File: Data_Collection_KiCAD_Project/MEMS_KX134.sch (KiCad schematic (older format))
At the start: 2 parts

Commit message: Fixed Component Libraries
Changed over from project specific to global libraries.
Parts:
- C?: symbol Data_Collection_KiCAD_Project-rescue:C_Small-Device -> Data_Collection_KiCAD_Project-rescue:C_Small-Device-Data_Collection_KiCAD_Project-rescue
- U?: symbol Data_Collection_KiCAD_Project-rescue:KX122-1042-Sensor_Motion -> Data_Collection_KiCAD_Project-rescue:KX122-1042-Sensor_Motion-Data_Collection_KiCAD_Project-rescue
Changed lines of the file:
@@
 $Descr A4 11693 8268
 encoding utf-8
-Sheet 9 10
+Sheet 9 9
 Title "ICM-20948 MEMS Chip"
 Date "2021-10-01"
@@
 $EndDescr
 $Comp
-L Data_Collection_KiCAD_Project-rescue:KX122-1042-Sensor_Motion U?
+L Data_Collection_KiCAD_Project-rescue:KX122-1042-Sensor_Motion-Data_Collection_KiCAD_Project-rescue U?
 U 1 1 6165C3D0
 P 5950 3450
@@
 SCL
 $Comp
-L Data_Collection_KiCAD_Project-rescue:GND-power #PWR?
+L Data_Collection_KiCAD_Project-rescue:GND-power-Data_Collection_KiCAD_Project-rescue #PWR?
 U 1 1 61692503
 P 5950 3950
@@
 $EndComp
 $Comp
-L Data_Collection_KiCAD_Project-rescue:+3.3V-power #PWR?
+L Data_Collection_KiCAD_Project-rescue:+3.3V-power-Data_Collection_KiCAD_Project-rescue #PWR?
 U 1 1 6169CC30
 P 5350 2900
@@
 $EndComp
 $Comp
-L Data_Collection_KiCAD_Project-rescue:C_Small-Device C?
+L Data_Collection_KiCAD_Project-rescue:C_Small-Device-Data_Collection_KiCAD_Project-rescue C?
 U 1 1 6169DA95
 P 6450 2900
@@
 $EndComp
 $Comp
-L Data_Collection_KiCAD_Project-rescue:GND-power #PWR?
+L Data_Collection_KiCAD_Project-rescue:GND-power-Data_Collection_KiCAD_Project-rescue #PWR?
 U 1 1 6169E39E
 P 6650 2900
@@
 KX134-1211 I2C Addresses:\nADDR = 0 -> 0x1E\nADDR = 1 -> 0x1F
 $Comp
-L Data_Collection_KiCAD_Project-rescue:GND-power #PWR?
+L Data_Collection_KiCAD_Project-rescue:GND-power-Data_Collection_KiCAD_Project-rescue #PWR?
 U 1 1 616ACA8D
 P 5200 3600
@@
 	5200 3450 5200 3600
 $Comp
-L Data_Collection_KiCAD_Project-rescue:GND-power #PWR?
+L Data_Collection_KiCAD_Project-rescue:GND-power-Data_Collection_KiCAD_Project-rescue #PWR?
 U 1 1 616AF0ED
 P 6700 3900

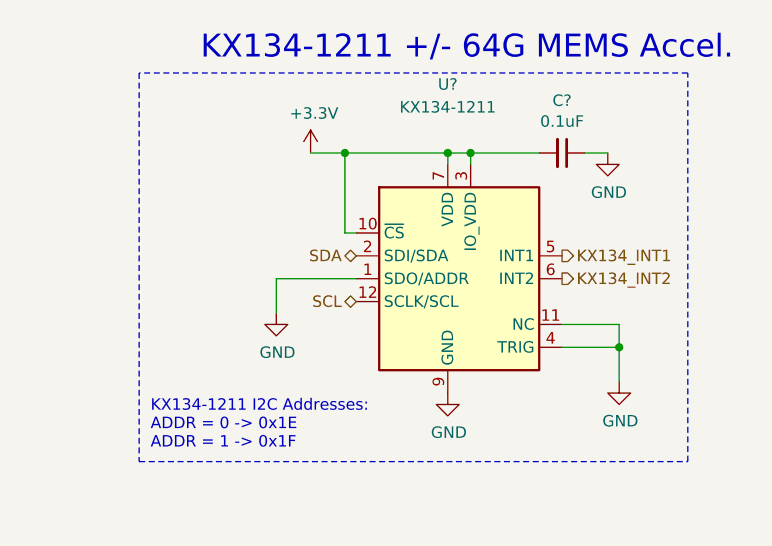
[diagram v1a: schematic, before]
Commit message: footprint and value changes
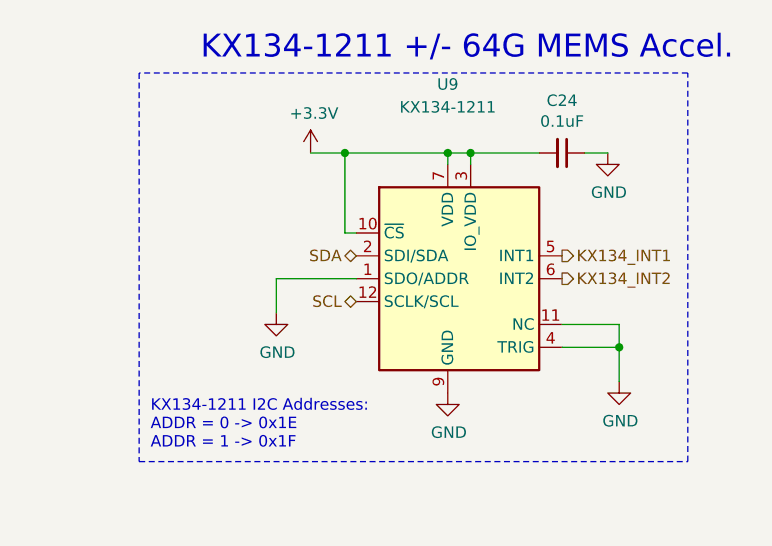
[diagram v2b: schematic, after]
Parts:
- C24: renamed from C?; footprint (none) -> Capacitor_SMD:C_0603_1608Metric
- gave numbers to parts that had none: 1
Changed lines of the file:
@@
 $EndDescr
 $Comp
-L Data_Collection_KiCAD_Project-rescue:KX122-1042-Sensor_Motion-Data_Collection_KiCAD_Project-rescue U?
+L Data_Collection_KiCAD_Project-rescue:KX122-1042-Sensor_Motion-Data_Collection_KiCAD_Project-rescue U9
 U 1 1 6165C3D0
 P 5950 3450
-F 0 "U?" H 5950 4300 50  0000 C CNN
+F 0 "U9" H 5950 4300 50  0000 C CNN
 F 1 "KX134-1211" H 5950 4200 50  0000 C CNN
 F 2 "Package_LGA:LGA-12_2x2mm_P0.5mm" H 6100 4000 50  0001 L CNN
@@
 SCL
 $Comp
-L Data_Collection_KiCAD_Project-rescue:GND-power-Data_Collection_KiCAD_Project-rescue #PWR?
+L Data_Collection_KiCAD_Project-rescue:GND-power-Data_Collection_KiCAD_Project-rescue #PWR056
 U 1 1 61692503
 P 5950 3950
-F 0 "#PWR?" H 5950 3700 50  0001 C CNN
+F 0 "#PWR056" H 5950 3700 50  0001 C CNN
 F 1 "GND" H 5955 3777 50  0000 C CNN
 F 2 "" H 5950 3950 50  0001 C CNN
@@
 $EndComp
 $Comp
-L Data_Collection_KiCAD_Project-rescue:+3.3V-power-Data_Collection_KiCAD_Project-rescue #PWR?
+L Data_Collection_KiCAD_Project-rescue:+3.3V-power-Data_Collection_KiCAD_Project-rescue #PWR055
 U 1 1 6169CC30
 P 5350 2900
-F 0 "#PWR?" H 5350 2750 50  0001 C CNN
+F 0 "#PWR055" H 5350 2750 50  0001 C CNN
 F 1 "+3.3V" H 5365 3073 50  0000 C CNN
 F 2 "" H 5350 2900 50  0001 C CNN
@@
 $EndComp
 $Comp
-L Data_Collection_KiCAD_Project-rescue:C_Small-Device-Data_Collection_KiCAD_Project-rescue C?
+L Data_Collection_KiCAD_Project-rescue:C_Small-Device-Data_Collection_KiCAD_Project-rescue C24
 U 1 1 6169DA95
 P 6450 2900
-F 0 "C?" V 6221 2900 50  0000 C CNN
+F 0 "C24" V 6221 2900 50  0000 C CNN
 F 1 "0.1uF" V 6312 2900 50  0000 C CNN
-F 2 "" H 6450 2900 50  0001 C CNN
+F 2 "Capacitor_SMD:C_0603_1608Metric" H 6450 2900 50  0001 C CNN
 F 3 "~" H 6450 2900 50  0001 C CNN
 	1    6450 2900
@@
 $EndComp
 $Comp
-L Data_Collection_KiCAD_Project-rescue:GND-power-Data_Collection_KiCAD_Project-rescue #PWR?
+L Data_Collection_KiCAD_Project-rescue:GND-power-Data_Collection_KiCAD_Project-rescue #PWR057
 U 1 1 6169E39E
 P 6650 2900
-F 0 "#PWR?" H 6650 2650 50  0001 C CNN
+F 0 "#PWR057" H 6650 2650 50  0001 C CNN
 F 1 "GND" H 6655 2727 50  0000 C CNN
 F 2 "" H 6650 2900 50  0001 C CNN
@@
 KX134-1211 I2C Addresses:\nADDR = 0 -> 0x1E\nADDR = 1 -> 0x1F
 $Comp
-L Data_Collection_KiCAD_Project-rescue:GND-power-Data_Collection_KiCAD_Project-rescue #PWR?
+L Data_Collection_KiCAD_Project-rescue:GND-power-Data_Collection_KiCAD_Project-rescue #PWR054
 U 1 1 616ACA8D
 P 5200 3600
-F 0 "#PWR?" H 5200 3350 50  0001 C CNN
+F 0 "#PWR054" H 5200 3350 50  0001 C CNN
 F 1 "GND" H 5205 3427 50  0000 C CNN
 F 2 "" H 5200 3600 50  0001 C CNN
@@
 	5200 3450 5200 3600
 $Comp
-L Data_Collection_KiCAD_Project-rescue:GND-power-Data_Collection_KiCAD_Project-rescue #PWR?
+L Data_Collection_KiCAD_Project-rescue:GND-power-Data_Collection_KiCAD_Project-rescue #PWR058
 U 1 1 616AF0ED
 P 6700 3900
-F 0 "#PWR?" H 6700 3650 50  0001 C CNN
+F 0 "#PWR058" H 6700 3650 50  0001 C CNN
 F 1 "GND" H 6705 3727 50  0000 C CNN
 F 2 "" H 6700 3900 50  0001 C CNN

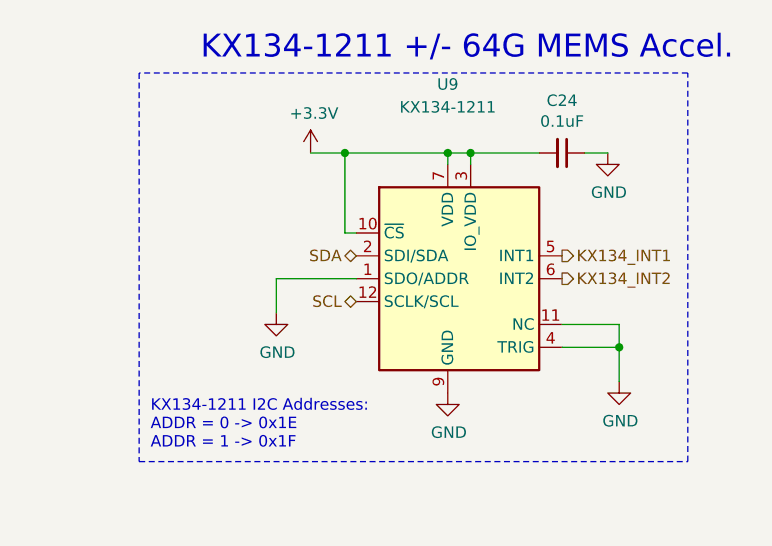
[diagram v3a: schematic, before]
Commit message: footprint changes
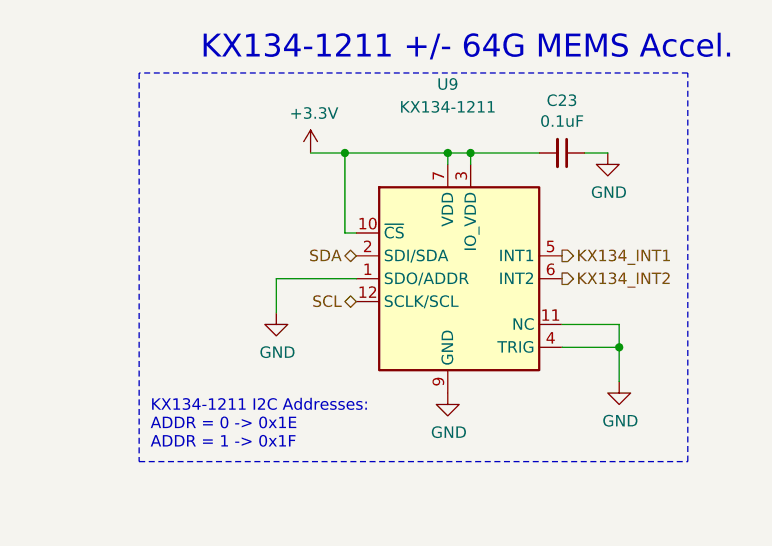
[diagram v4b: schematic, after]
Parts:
- renumbered C24 to C23
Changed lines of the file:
@@
 SCL
 $Comp
-L Data_Collection_KiCAD_Project-rescue:GND-power-Data_Collection_KiCAD_Project-rescue #PWR056
+L Data_Collection_KiCAD_Project-rescue:GND-power-Data_Collection_KiCAD_Project-rescue #PWR049
 U 1 1 61692503
 P 5950 3950
-F 0 "#PWR056" H 5950 3700 50  0001 C CNN
+F 0 "#PWR049" H 5950 3700 50  0001 C CNN
 F 1 "GND" H 5955 3777 50  0000 C CNN
 F 2 "" H 5950 3950 50  0001 C CNN
@@
 $EndComp
 $Comp
-L Data_Collection_KiCAD_Project-rescue:+3.3V-power-Data_Collection_KiCAD_Project-rescue #PWR055
+L Data_Collection_KiCAD_Project-rescue:+3.3V-power-Data_Collection_KiCAD_Project-rescue #PWR048
 U 1 1 6169CC30
 P 5350 2900
-F 0 "#PWR055" H 5350 2750 50  0001 C CNN
+F 0 "#PWR048" H 5350 2750 50  0001 C CNN
 F 1 "+3.3V" H 5365 3073 50  0000 C CNN
 F 2 "" H 5350 2900 50  0001 C CNN
@@
 $EndComp
 $Comp
-L Data_Collection_KiCAD_Project-rescue:C_Small-Device-Data_Collection_KiCAD_Project-rescue C24
+L Data_Collection_KiCAD_Project-rescue:C_Small-Device-Data_Collection_KiCAD_Project-rescue C23
 U 1 1 6169DA95
 P 6450 2900
-F 0 "C24" V 6221 2900 50  0000 C CNN
+F 0 "C23" V 6221 2900 50  0000 C CNN
 F 1 "0.1uF" V 6312 2900 50  0000 C CNN
 F 2 "Capacitor_SMD:C_0603_1608Metric" H 6450 2900 50  0001 C CNN
@@
 $EndComp
 $Comp
-L Data_Collection_KiCAD_Project-rescue:GND-power-Data_Collection_KiCAD_Project-rescue #PWR057
+L Data_Collection_KiCAD_Project-rescue:GND-power-Data_Collection_KiCAD_Project-rescue #PWR050
 U 1 1 6169E39E
 P 6650 2900
-F 0 "#PWR057" H 6650 2650 50  0001 C CNN
+F 0 "#PWR050" H 6650 2650 50  0001 C CNN
 F 1 "GND" H 6655 2727 50  0000 C CNN
 F 2 "" H 6650 2900 50  0001 C CNN
@@
 KX134-1211 I2C Addresses:\nADDR = 0 -> 0x1E\nADDR = 1 -> 0x1F
 $Comp
-L Data_Collection_KiCAD_Project-rescue:GND-power-Data_Collection_KiCAD_Project-rescue #PWR054
+L Data_Collection_KiCAD_Project-rescue:GND-power-Data_Collection_KiCAD_Project-rescue #PWR047
 U 1 1 616ACA8D
 P 5200 3600
-F 0 "#PWR054" H 5200 3350 50  0001 C CNN
+F 0 "#PWR047" H 5200 3350 50  0001 C CNN
 F 1 "GND" H 5205 3427 50  0000 C CNN
 F 2 "" H 5200 3600 50  0001 C CNN
@@
 	5200 3450 5200 3600
 $Comp
-L Data_Collection_KiCAD_Project-rescue:GND-power-Data_Collection_KiCAD_Project-rescue #PWR058
+L Data_Collection_KiCAD_Project-rescue:GND-power-Data_Collection_KiCAD_Project-rescue #PWR051
 U 1 1 616AF0ED
 P 6700 3900
-F 0 "#PWR058" H 6700 3650 50  0001 C CNN
+F 0 "#PWR051" H 6700 3650 50  0001 C CNN
 F 1 "GND" H 6705 3727 50  0000 C CNN
 F 2 "" H 6700 3900 50  0001 C CNN
